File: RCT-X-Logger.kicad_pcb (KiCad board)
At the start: 2 copper layers, 30 x 70 mm, 68 parts, among them J1 USB_B_Micro, P1 KRC_Conn_SWD, U1 KRC_Conn_CAN, U2 LT1761-5, U3 LT1965xDD-3.3, U4 NCV7342, U5 CY8C58xxLTI-LPxxx, U6 CAM-M8C, U7 MS5607, U8 W25N01GVxxIG-IT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

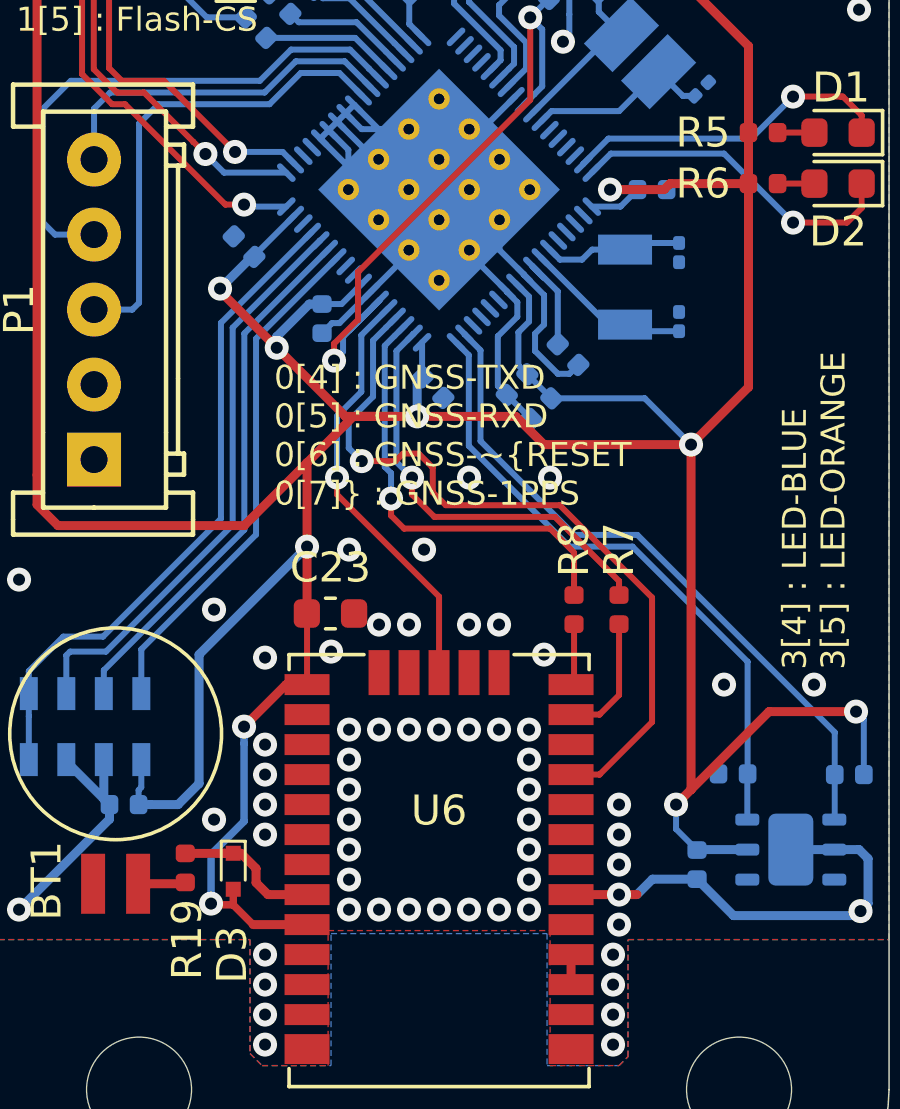
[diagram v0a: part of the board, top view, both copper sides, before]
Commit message: [update]moved capacitor placement
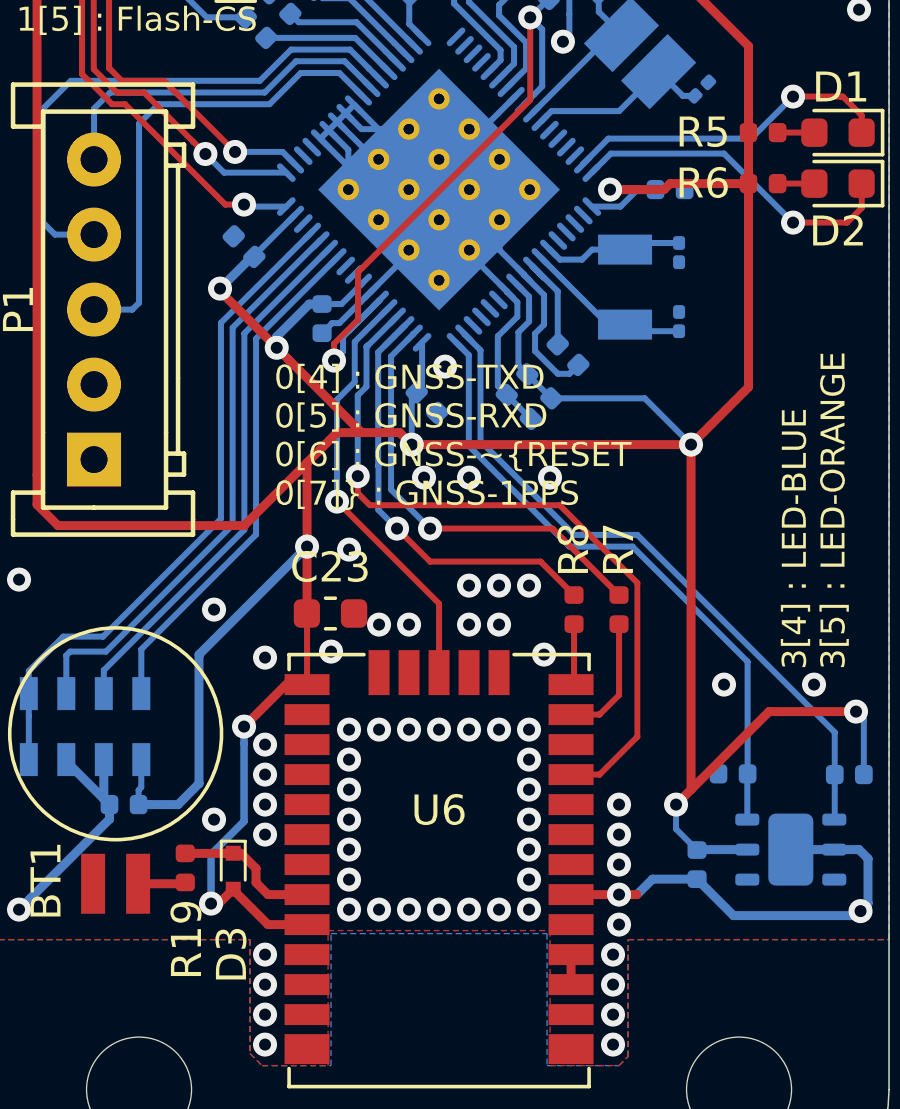
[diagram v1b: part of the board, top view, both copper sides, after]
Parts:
- moved C13 0.60 mm to (62.7, 95.0)
- moved C12 0.54 mm to (54.6, 102.1)
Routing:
- net /GNSS-~RESET: track 25.5 -> 24.8 mm
- net GND: vias 70 -> 74
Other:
- board text removed: "0[4] : GNSS-TXD 0[5] : GNSS-RXD 0[6] : GNSS-~RESET 0[7] : GNSS-1PPS 1[2] : Flash-SCLK 1[3] : Flash-MOSI 1[4] : Flash-MISO 1[5] : Flash-~CS 2[0] : PT-SCLK 2[1] : PT-MOSI 2[2] : PT-MISO 2[3] : PT-~CS"

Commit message: Completed Rev2
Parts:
- removed D3: D, KUTKiCad_footprint:D_SOD-723
- removed the G*** at (63.2, 75.2)
- added F1: Polyfuse, Fuse:Fuse_0805_2012Metric, B.Cu at (57.2, 76.6)
- added J2: Conn_01x02, Connector_JST:JST_XH_B2B-XH-A_1x02_P2.50mm_Vertical, F.Cu at (66.0, 105.8)
- added R20: 68kΩ, Resistor_SMD:R_0402_1005Metric, F.Cu at (46.8, 116.3)
- D1: value LED_BLUE -> LED_RGBA; footprint LED_SMD:LED_0603_1608Metric -> KUTKiCad_footprint:LED_LiteOn_LTST-C19HE1WT
- D2: value LED_OR -> D; footprint LED_SMD:LED_0603_1608Metric -> KUTKiCad_footprint:D_SOD-723
- G***, R9: moved to F.Cu
- H1, H2, H3, H4: footprint MountingHole:MountingHole_3.5mm -> MountingHole:MountingHole_3.2mm_M3
- R13: value 4.7kΩ -> 22Ω
- R19: value 68kΩ -> 4.7kΩ; moved to B.Cu
- R5: value 220Ω -> 1.5kΩ
- R6, R7: value 220Ω -> 820Ω
- R8: value 220Ω -> 22Ω
- U6: value CAM-M8C -> MS5611; footprint KUTKiCad_footprint:ublox-CAM -> KUTKiCad_footprint:TE_Sensor_MS8607; moved to B.Cu
- U7: value MS5607 -> CAM-M8C; footprint KUTKiCad_footprint:TE_Sensor_MS8607 -> KUTKiCad_footprint:ublox-CAM; moved to F.Cu
- U8: value W25N01GVxxIG-IT -> HTU21D; footprint KUTKiCad_footprint:WSON-8_8x6mm_P1.27mm -> Package_DFN_QFN:DFN-6-1EP_3x3mm_P1mm_EP1.5x2.4mm
- U9: value HTU21D -> W25N01GVxxIG-IT; footprint Package_DFN_QFN:DFN-6-1EP_3x3mm_P1mm_EP1.5x2.4mm -> KUTKiCad_footprint:WSON-8_8x6mm_P1.27mm
- moved G*** 58.4 mm to (55.0, 128.9), turned to 0 degrees
- moved R15 42.7 mm to (41.1, 81.9), turned to 90 degrees
- moved U8 39.6 mm to (66.7, 117.0)
- moved U9 39.6 mm to (46.5, 83.0)
- moved R16 36.3 mm to (64.8, 114.5), turned to 180 degrees
- moved R14 34.6 mm to (68.7, 114.5), turned to 0 degrees
- moved R19 34.1 mm to (53.1, 84.1), turned to 270 degrees
- moved R17 33.0 mm to (51.9, 84.1), turned to 270 degrees
- moved D2 31.3 mm to (47.3, 118.0), turned to 270 degrees
- moved R9 22.8 mm to (59.5, 109.0), turned to 90 degrees
- moved U6 16.7 mm to (43.2, 112.9), turned to 90 degrees
- moved U7 16.7 mm to (59.8, 110.7), turned to 180 degrees
- moved R7 14.8 mm to (67.0, 95.5), turned to 0 degrees
- moved R13 11.2 mm to (50.6, 87.8), turned to 315 degrees
- moved R12 5.48 mm to (45.9, 87.8)
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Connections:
- D2 pad 2: Net-(D2-Pad2) -> +3V3
- R10 pad 2: /Flash-MOSI -> /Flash-MISO
- R11 pad 2: /Flash-SCLK -> /Flash-MOSI
- R12 pad 2: /Flash-~CS -> /Flash-SCLK
- R13 pad 2: +3V3 -> /Flash-~CS
- R14 pad 1: Net-(R14-Pad1) -> /H-SDA
- R15 pad 1: /H-SDA -> Net-(R15-Pad1)
- R16 pad 1: Net-(R12-Pad1) -> /H-SCL
- R17 pad 1: /H-SCL -> Net-(R17-Pad1)
- R18 pad 1: Net-(R18-Pad1) -> Net-(R13-Pad1)
- R19 pad 1: Net-(BT1-Pad1) -> Net-(R10-Pad1)
- R19 pad 2: Net-(D3-Pad1) -> +3V3
- R5 pad 1: Net-(D1-Pad2) -> Net-(R5-Pad1)
- R5 pad 2: +3V3 -> Net-(D1-Pad1)
- R6 pad 1: Net-(D2-Pad2) -> Net-(R6-Pad1)
- R6 pad 2: +3V3 -> Net-(D1-Pad2)
- R7 pad 2: /GNSS-TXD -> Net-(D1-Pad3)
- R8 pad 2: /GNSS-RXD -> /GNSS-TXD
- R9 pad 1: Net-(R18-Pad1) -> Net-(R9-Pad1)
- R9 pad 2: /Flash-MISO -> /GNSS-RXD
- U1 pad 2: Net-(C1-Pad1) -> Net-(F1-Pad2)
- U5 pad 32: Net-(U5-Pad32) -> Net-(R5-Pad1)
- U5 pad 33: Net-(D1-Pad1) -> Net-(R6-Pad1)
- U5 pad 34: Net-(D2-Pad1) -> Net-(R7-Pad1)
- U6 pad 2: Net-(U6-Pad2) -> GND
- U6 pad 3: Net-(U6-Pad3) -> GND
- U6 pad 4: GND -> /PT-~CS
- U6 pad 5: GND -> /PT-~CS
- U6 pad 6: Net-(U6-Pad6) -> /PT-MISO
- U6 pad 7: Net-(U6-Pad7) -> /PT-MOSI
- U6 pad 8: Net-(D3-Pad1) -> /PT-SCLK
- U7 pad 2: GND -> Net-(U7-Pad2)
- U7 pad 3: GND -> Net-(U7-Pad3)
- U7 pad 4: /PT-~CS -> GND
- U7 pad 5: /PT-~CS -> GND
- U7 pad 6: /PT-MISO -> Net-(U7-Pad6)
- U7 pad 7: /PT-MOSI -> Net-(U7-Pad7)
- U7 pad 8: /PT-SCLK -> Net-(D2-Pad1)
- U8 pad 1: Net-(R12-Pad1) -> /H-SDA
- U8 pad 2: Net-(R18-Pad1) -> GND
- U8 pad 3: Net-(R14-Pad1) -> Net-(U8-Pad3)
- U8 pad 4: GND -> Net-(U8-Pad4)
- U8 pad 5: Net-(R10-Pad1) -> +3V3
- U8 pad 6: Net-(R11-Pad1) -> /H-SCL
- U8 pad 7: Net-(R13-Pad1) -> GND
- U9 pad 1: /H-SDA -> Net-(R13-Pad1)
- U9 pad 2: GND -> Net-(R10-Pad1)
- U9 pad 3: Net-(U9-Pad3) -> Net-(R17-Pad1)
- U9 pad 4: Net-(U9-Pad4) -> GND
- U9 pad 5: +3V3 -> Net-(R11-Pad1)
- U9 pad 6: /H-SCL -> Net-(R12-Pad1)
- U9 pad 7: GND -> Net-(R15-Pad1)
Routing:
- net GND: track 60.6 -> 40.1 mm, vias 74 -> 135
- net /GNSS-1PPS: track 14.3 -> 31.2 mm
- net +3V3: track 241.4 -> 226.3 mm
- net Net-(R18-Pad1): track 13.6 -> 0.00 mm
- net Net-(R13-Pad1): track 1.37 -> 13.7 mm
- net Net-(D1-Pad1): track 11.1 -> 1.45 mm, vias 1 -> 0
- net Net-(R5-Pad1): track 0.00 -> 7.56 mm, vias 0 -> 1
- net Net-(R6-Pad1): track 0.00 -> 7.05 mm, vias 0 -> 1
- net Net-(R11-Pad1): track 12.7 -> 5.99 mm
- net Net-(R12-Pad1): track 14.6 -> 7.84 mm
- net Net-(C1-Pad1): track 32.9 -> 39.6 mm, vias 0 -> 2
- net Net-(D2-Pad1): track 11.2 -> 4.84 mm, vias 1 -> 0
- net +5V: track 9.03 -> 14.4 mm
- net Net-(R1-Pad2): track 19.3 -> 24.6 mm
- net /CAN-RXD: track 20.5 -> 15.4 mm
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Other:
- board text added: "3[3] : LED-RED 3[4] : LED-GREEN 3[5] : LED-BLUE"
- board text added: "Rev2"
- board text removed: "3[4] : LED-BLUE 3[5] : LED-ORANGE"
- board text removed: "Rev1.0.0"
